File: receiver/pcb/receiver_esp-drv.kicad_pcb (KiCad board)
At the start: 2 copper layers, 39 x 43.2 mm, 20 parts, among them J1 Conn_01x02_Female, J2 Conn_01x02_Female, J3 Conn_01x02_Female, J4 Conn_01x01_Female-weapon, J5 Conn_01x01_Female-weapon, U1 DRV8870DDA, U2 DRV8870DDA, U3 AMS1117-3.3, U4 ESP32-C3-MINI-1

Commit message: increase trace width on receiver pcb
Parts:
- renumbered J1 to Batt1, J2 to M1, J3 to M2
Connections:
- U1 pad 7: unconnected-(U1-Pad7) -> GND
- U2 pad 7: unconnected-(U2-Pad7) -> GND
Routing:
- net GND: track 97.8 -> 108.5 mm
- net +12V: track 79.7 -> 83.0 mm

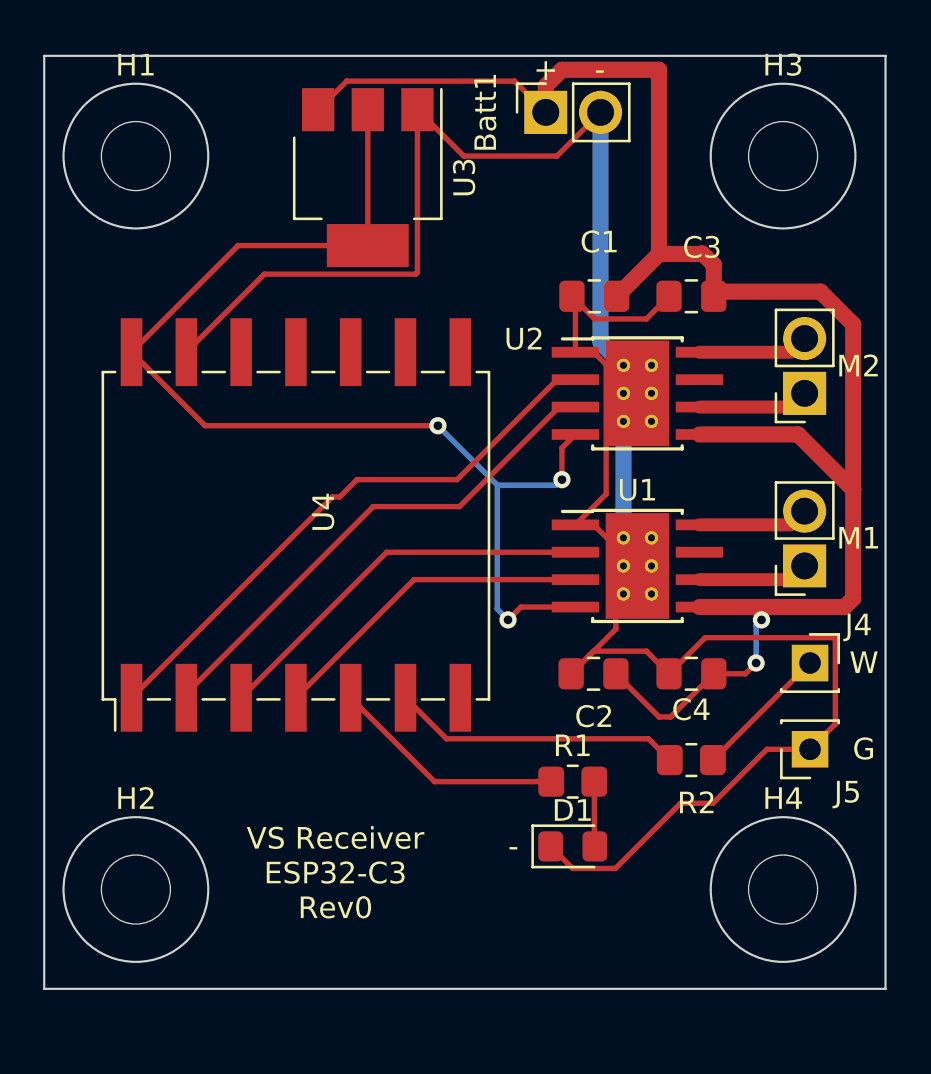
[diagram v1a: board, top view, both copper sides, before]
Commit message: add logo footprint
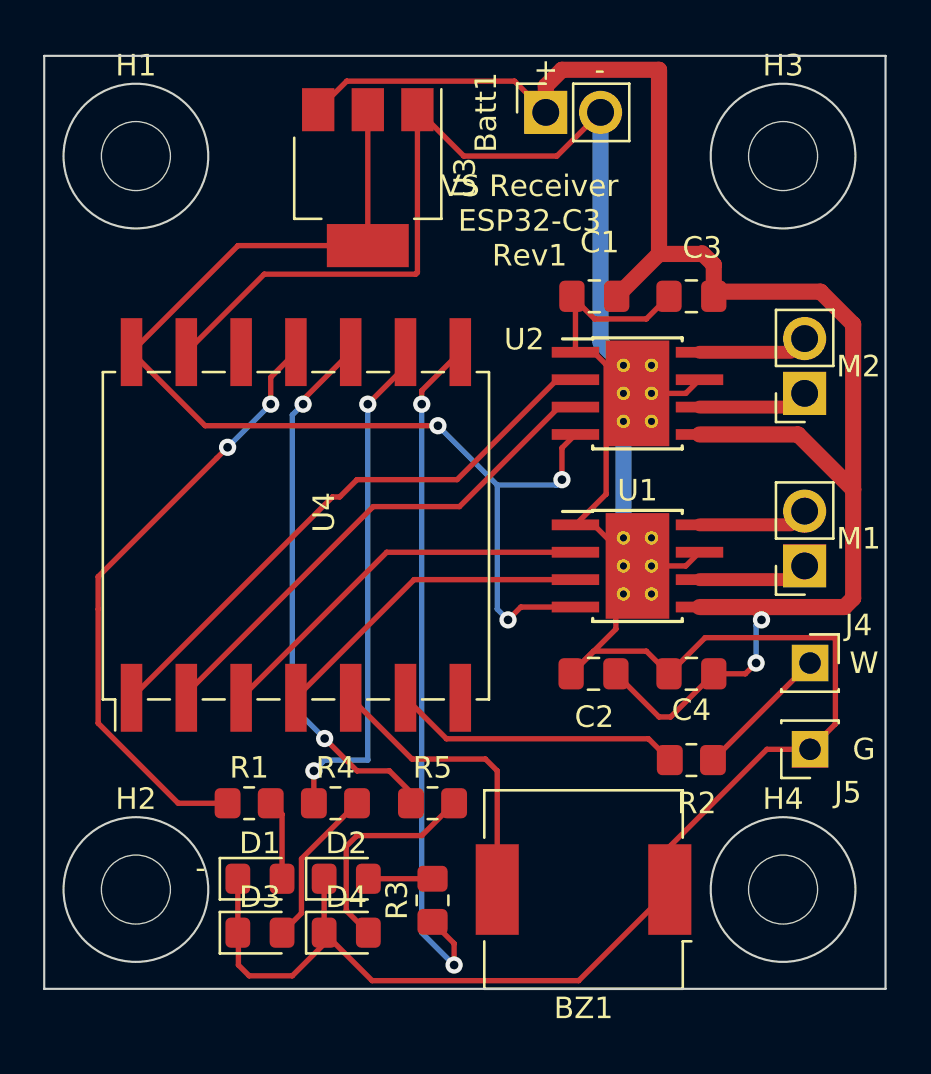
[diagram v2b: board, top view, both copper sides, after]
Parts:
- added BZ1: Buzzer, Buzzer_Beeper:Buzzer_CUI_CPT-9019S-SMT, F.Cu at (171.5, 115.0)
- added D2: LED, LED_SMD:LED_0805_2012Metric_Pad1.15x1.40mm_HandSolder, F.Cu at (160.5, 114.5)
- added D3: LED, LED_SMD:LED_0805_2012Metric_Pad1.15x1.40mm_HandSolder, F.Cu at (156.5, 117.0)
- added D4: LED, LED_SMD:LED_0805_2012Metric_Pad1.15x1.40mm_HandSolder, F.Cu at (160.5, 117.0)
- added G***: LOGO, VS-Logo:VS-Logo, B.Cu at (166.0, 99.0)
- added R3: 680 ohm, Resistor_SMD:R_0805_2012Metric_Pad1.20x1.40mm_HandSolder, F.Cu at (164.5, 115.5)
- added R4: 680 ohm, Resistor_SMD:R_0805_2012Metric_Pad1.20x1.40mm_HandSolder, F.Cu at (160.0, 111.0)
- added R5: 680 ohm, Resistor_SMD:R_0805_2012Metric_Pad1.20x1.40mm_HandSolder, F.Cu at (164.5, 111.0)
- moved R1 15.0 mm to (156.0, 111.0)
- moved D1 14.6 mm to (156.5, 114.5)
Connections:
- R1 pad 1: Net-(R1-Pad1) -> /LED1
- U4 pad 16: unconnected-(U4-Pad16) -> /LED1
- U4 pad 18: Net-(R1-Pad1) -> /spkr
- U4 pad 21: unconnected-(U4-Pad21) -> /LED2
- U4 pad 22: unconnected-(U4-Pad22) -> /LED3
- U4 pad 23: unconnected-(U4-Pad23) -> /LED4
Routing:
- net /LED2: track 0.00 -> 32.2 mm, vias 0 -> 2
- net GND: track 108.5 -> 139.7 mm
- net /LED1: track 0.00 -> 28.5 mm, vias 0 -> 2
- net /LED4: track 0.00 -> 25.2 mm, vias 0 -> 2
- net /LED3: track 0.00 -> 23.8 mm, vias 0 -> 2
- net /spkr: track 0.00 -> 13.7 mm
- net Net-(R1-Pad1): track 10.9 -> 0.00 mm
- net Net-(D4-Pad2): track 0.00 -> 10.3 mm
- net Net-(D3-Pad2): track 0.00 -> 7.44 mm
- net Net-(D2-Pad2): track 0.00 -> 2.97 mm
- net Net-(D1-Pad2): track 3.01 -> 3.75 mm
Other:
- board text added: "VS Receiver ESP32-C3 Rev1"
- board text removed: "VS Receiver ESP32-C3 Rev0"
